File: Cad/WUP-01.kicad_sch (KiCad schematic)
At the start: 23 parts, among them P1 USB_A_Stacked, P1013 Power, P11 Fan connector, P12 FRT, P13 Bluetooth, P2 USB_A_Side2side, P4 HDMI_A, P5 Micro_SD_Card_Det2, P6 5GHz, P7 2.4GHz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

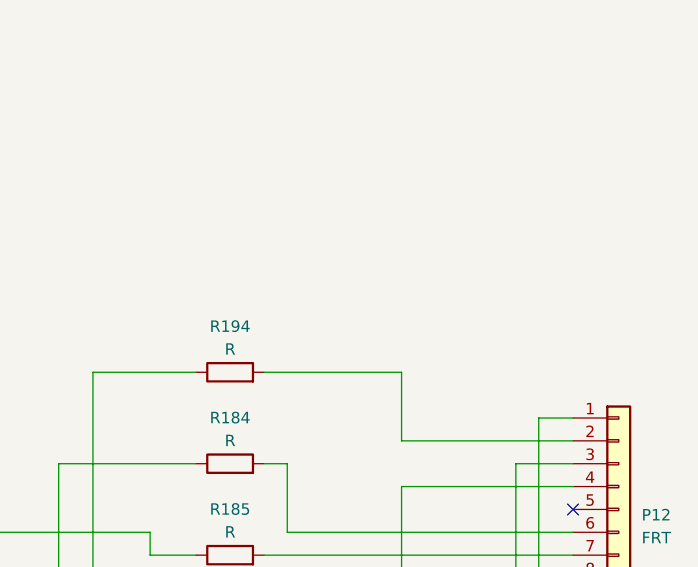
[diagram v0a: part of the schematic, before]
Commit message: Added notes on a schematic
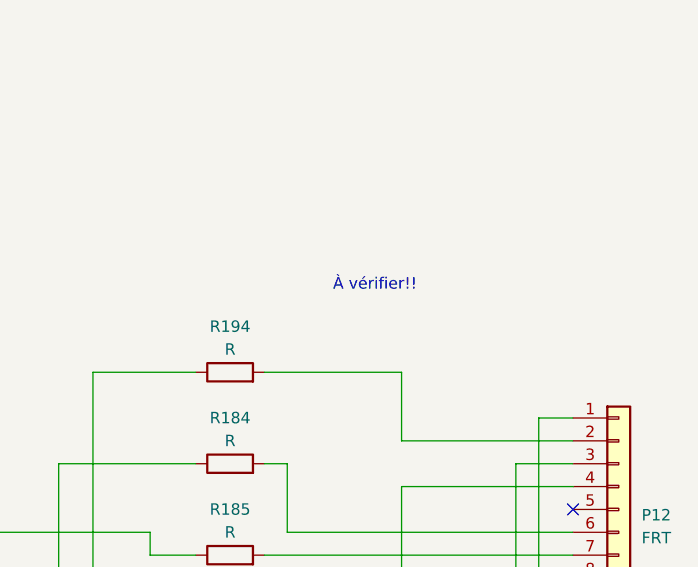
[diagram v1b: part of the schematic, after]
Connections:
- net at U8. (9): now also R184.1
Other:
- note added: "À vérifier!!"
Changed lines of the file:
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@@
     (stroke (width 0) (type default))
+  )
+  (text "À vérifier!!\n" (at 326.39 97.79 0)
+    (effects (font (size 1.27 1.27)) (justify left bottom))
   )
   (symbol (lib_id "power:GND") (at 317.5 156.21 0) (unit 1)
